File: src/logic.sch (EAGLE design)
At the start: 68 parts, among them CON1 CON-4P-TABS-JST_GH-RA, CON11 PINHEAD_1X03-2, CON12 PINHEAD_1X03-2, CON2 PINHEAD_1X04-2.54, CON3 PINHEAD_2X04-PLS-2, CON6 PINHEAD_2X02-PTH-2-MALE, CON7 PINHEAD_2X02-PTH-2-MALE, IC1 STM32F105RCT6, IC10 LM75-TSSOP8, IC11 LM75-TSSOP8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

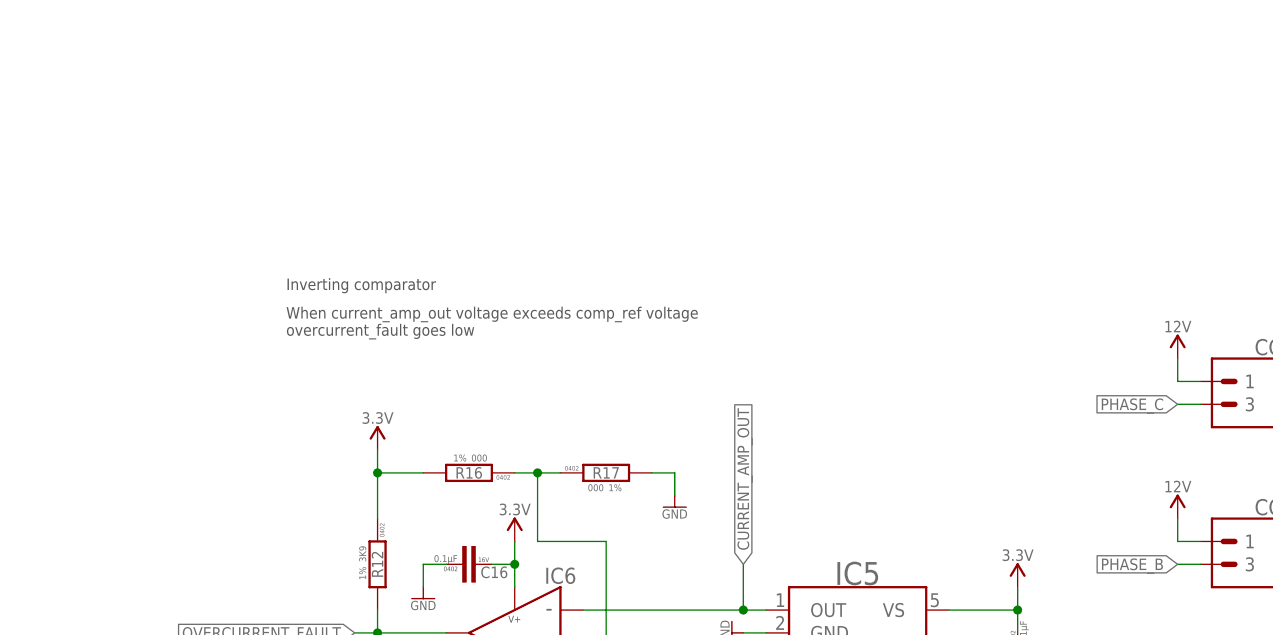
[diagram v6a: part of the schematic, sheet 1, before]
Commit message: experimental digital pot added
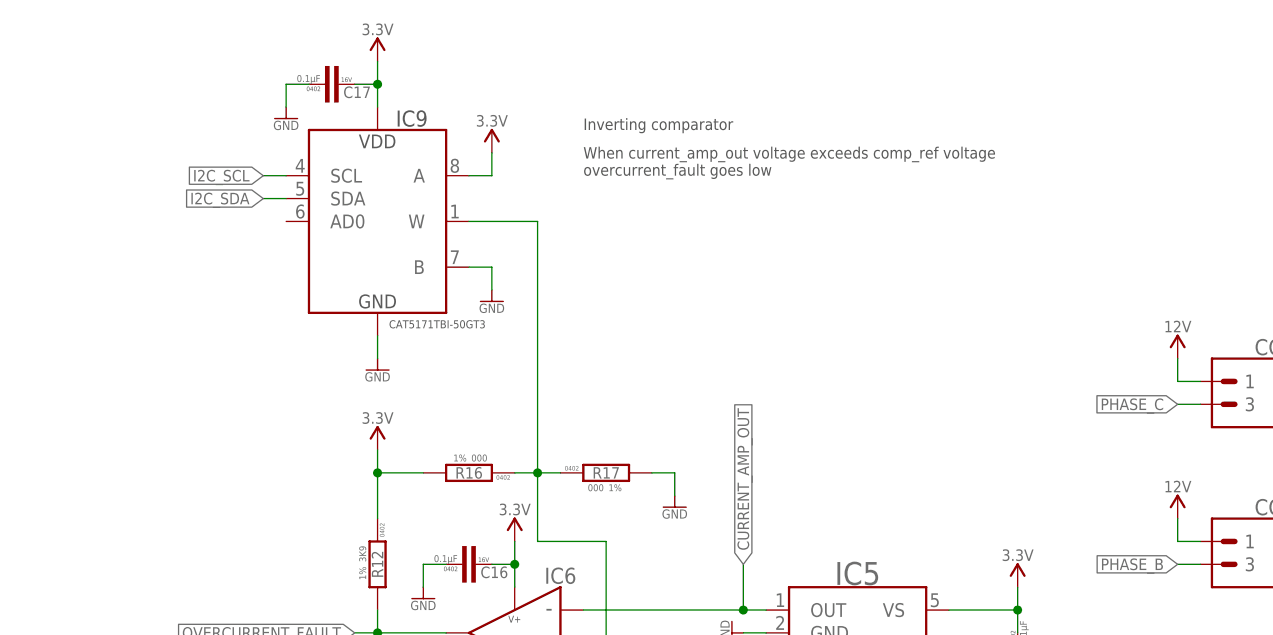
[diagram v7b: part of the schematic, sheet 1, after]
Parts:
- added C17: 0.1µF, rc:C-0402
- added IC9: CAT5171TBI-50GT3, misc:CAT5171TBI-50GT3
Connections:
- net GND: now also C17.1, IC9.B, IC9.GND
- net I2C_SCL: now also IC9.SCL
- net I2C_SDA: now also IC9.SDA
- net N$2: now also IC9.W
- net VDD_3V3: now also C17.2, IC9.A, IC9.VDD
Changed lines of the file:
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@@
 </part>
 <part name="GND44" library="supply_symbols" library_urn="urn:adsk.eagle:library:13097679" deviceset="GND" device="" value="GND"/>
+<part name="IC9" library="misc" library_urn="urn:adsk.eagle:library:5347860" deviceset="CAT5171TBI" device="" package3d_urn="urn:adsk.eagle:package:24574323/1" technology="-50GT3"/>
+<part name="C17" library="rc" library_urn="urn:adsk.eagle:library:2539423" deviceset="C" device="-0402" package3d_urn="urn:adsk.eagle:package:2539461/2" value="0.1µF">
+<attribute name="AEC-Q" value="---"/>
+<attribute name="DIGIKEY#" value="490-3261-1-ND"/>
+<attribute name="MANF" value="Murata Electronics"/>
+<attribute name="MANF#" value="GRM155R71C104KA88D"/>
+<attribute name="OPERATING_TEMP" value="-55°C ~ 125°C"/>
+<attribute name="VOLTAGE" value="16V"/>
+</part>
+<part name="P+18" library="supply_symbols" library_urn="urn:adsk.eagle:library:13097679" deviceset="3.3V" device=""/>
+<part name="GND45" library="supply_symbols" library_urn="urn:adsk.eagle:library:13097679" deviceset="GND" device="" value="GND"/>
+<part name="GND46" library="supply_symbols" library_urn="urn:adsk.eagle:library:13097679" deviceset="GND" device="" value="GND"/>
+<part name="GND47" library="supply_symbols" library_urn="urn:adsk.eagle:library:13097679" deviceset="GND" device="" value="GND"/>
+<part name="P+19" library="supply_symbols" library_urn="urn:adsk.eagle:library:13097679" deviceset="3.3V" device=""/>
 </parts>
 <sheets>
@@
 <text x="142.24" y="55.88" size="1.27" layer="97" font="vector">Place R26 TO WRITE PROTECT</text>
 <text x="142.24" y="33.02" size="1.778" layer="97">WP pin pull up is optional</text>
-<text x="96.52" y="226.06" size="1.27" layer="97" font="vector">Inverting comparator</text>
-<text x="96.52" y="220.98" size="1.27" layer="97" font="vector">When current_amp_out voltage exceeds comp_ref voltage
+<text x="129.54" y="243.84" size="1.27" layer="97" font="vector">Inverting comparator</text>
+<text x="129.54" y="238.76" size="1.27" layer="97" font="vector">When current_amp_out voltage exceeds comp_ref voltage
 overcurrent_fault goes low</text>
 </plain>
@@
 <instance part="GND44" gate="1" x="139.7" y="203.2" smashed="yes">
 <attribute name="VALUE" x="139.7" y="201.168" size="1.016" layer="96" font="vector" ratio="15" align="center"/>
+</instance>
+<instance part="IC9" gate="G$1" x="99.06" y="223.52" smashed="yes">
+<attribute name="NAME" x="110.49" y="245.11" size="1.778" layer="97" font="vector" ratio="15" align="center"/>
+<attribute name="MANF#" x="107.95" y="222.25" size="0.889" layer="97" font="vector" ratio="15" align="center-left"/>
+</instance>
+<instance part="C17" gate="G$1" x="101.6" y="248.92" smashed="yes">
+<attribute name="NAME" x="102.87" y="248.031" size="1.27" layer="95" font="vector" align="center-left"/>
+<attribute name="VALUE" x="100.33" y="249.174" size="0.762" layer="96" font="vector" align="bottom-right"/>
+<attribute name="PACKAGE" x="99.568" y="248.412" size="0.508" layer="97" font="vector" rot="R180" align="center"/>
+<attribute name="VOLTAGE" x="102.616" y="249.428" size="0.508" layer="97" font="vector" align="center-left"/>
+</instance>
+<instance part="P+18" gate="G$1" x="106.68" y="251.46" smashed="yes" rot="MR0">
+<attribute name="VALUE" x="106.68" y="255.016" size="1.27" layer="96" font="vector" ratio="15" rot="MR0" align="center"/>
+</instance>
+<instance part="GND45" gate="1" x="106.68" y="218.44" smashed="yes">
+<attribute name="VALUE" x="106.68" y="216.408" size="1.016" layer="96" font="vector" ratio="15" align="center"/>
+</instance>
+<instance part="GND46" gate="1" x="96.52" y="246.38" smashed="yes">
+<attribute name="VALUE" x="96.52" y="244.348" size="1.016" layer="96" font="vector" ratio="15" align="center"/>
+</instance>
+<instance part="GND47" gate="1" x="119.38" y="226.06" smashed="yes">
+<attribute name="VALUE" x="119.38" y="224.028" size="1.016" layer="96" font="vector" ratio="15" align="center"/>
+</instance>
+<instance part="P+19" gate="G$1" x="119.38" y="241.3" smashed="yes" rot="MR0">
+<attribute name="VALUE" x="119.38" y="244.856" size="1.27" layer="96" font="vector" ratio="15" rot="MR0" align="center"/>
 </instance>
 </instances>
@@
 <wire x1="139.7" y1="203.2" x2="139.7" y2="205.74" width="0.1524" layer="91"/>
 <wire x1="139.7" y1="205.74" x2="137.16" y2="205.74" width="0.1524" layer="91"/>
+</segment>
+<segment>
+<pinref part="GND45" gate="1" pin="GND"/>
+<pinref part="IC9" gate="G$1" pin="GND"/>
+<wire x1="106.68" y1="218.44" x2="106.68" y2="220.98" width="0.1524" layer="91"/>
+</segment>
+<segment>
+<pinref part="GND46" gate="1" pin="GND"/>
+<wire x1="96.52" y1="246.38" x2="96.52" y2="248.92" width="0.1524" layer="91"/>
+<pinref part="C17" gate="G$1" pin="1"/>
+<wire x1="96.52" y1="248.92" x2="99.06" y2="248.92" width="0.1524" layer="91"/>
+</segment>
+<segment>
+<pinref part="GND47" gate="1" pin="GND"/>
+<wire x1="119.38" y1="226.06" x2="119.38" y2="228.6" width="0.1524" layer="91"/>
+<pinref part="IC9" gate="G$1" pin="B"/>
+<wire x1="119.38" y1="228.6" x2="116.84" y2="228.6" width="0.1524" layer="91"/>
 </segment>
 </net>
@@
 <label x="149.86" y="50.8" size="1.27" layer="95" rot="R180" xref="yes"/>
 </segment>
+<segment>
+<pinref part="IC9" gate="G$1" pin="SCL"/>
+<wire x1="96.52" y1="238.76" x2="93.98" y2="238.76" width="0.1524" layer="91"/>
+<label x="93.98" y="238.76" size="1.27" layer="95" rot="R180" xref="yes"/>
+</segment>
 </net>
 <net name="I2C_SDA" class="0">
@@
 <wire x1="152.4" y1="40.64" x2="149.86" y2="40.64" width="0.1524" layer="91"/>
 <label x="149.86" y="40.64" size="1.27" layer="95" rot="R180" xref="yes"/>
+</segment>
+<segment>
+<pinref part="IC9" gate="G$1" pin="SDA"/>
+<wire x1="96.52" y1="236.22" x2="93.98" y2="236.22" width="0.1524" layer="91"/>
+<label x="93.98" y="236.22" size="1.27" layer="95" rot="R180" xref="yes"/>
 </segment>
 </net>
@@
 <junction x="106.68" y="205.74"/>
 </segment>
+<segment>
+<pinref part="IC9" gate="G$1" pin="VDD"/>
+<wire x1="106.68" y1="246.38" x2="106.68" y2="248.92" width="0.1524" layer="91"/>
+<pinref part="C17" gate="G$1" pin="2"/>
+<wire x1="106.68" y1="248.92" x2="104.14" y2="248.92" width="0.1524" layer="91"/>
+<wire x1="106.68" y1="248.92" x2="106.68" y2="251.46" width="0.1524" layer="91"/>
+<junction x="106.68" y="248.92"/>
+<pinref part="P+18" gate="G$1" pin="VDD_3V3"/>
+</segment>
+<segment>
+<pinref part="P+19" gate="G$1" pin="VDD_3V3"/>
+<wire x1="119.38" y1="241.3" x2="119.38" y2="238.76" width="0.1524" layer="91"/>
+<pinref part="IC9" gate="G$1" pin="A"/>
+<wire x1="119.38" y1="238.76" x2="116.84" y2="238.76" width="0.1524" layer="91"/>
+</segment>
 </net>
 <net name="BOOT0" class="0">
@@
 <wire x1="132.08" y1="198.12" x2="132.08" y2="185.42" width="0.1524" layer="91"/>
 <junction x="132.08" y="185.42"/>
-</segment>
-</net>
+<pinref part="IC9" gate="G$1" pin="W"/>
+<wire x1="116.84" y1="233.68" x2="124.46" y2="233.68" width="0.1524" layer="91"/>
+<wire x1="124.46" y1="233.68" x2="124.46" y2="205.74" width="0.1524" layer="91"/>
+</segment>
+</net>

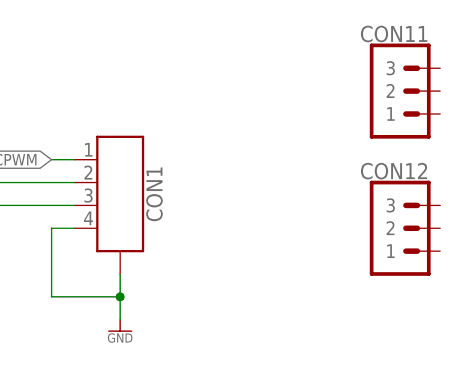
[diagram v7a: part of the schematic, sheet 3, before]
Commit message: bigger connector PCB connectors
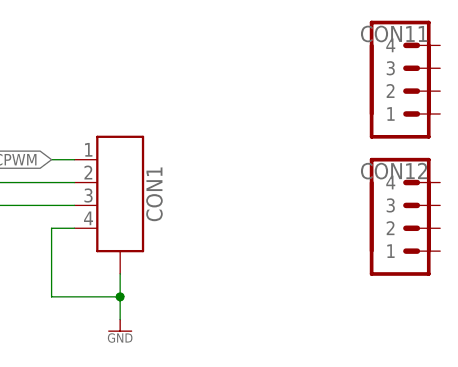
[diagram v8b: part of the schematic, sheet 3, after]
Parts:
- CON11, CON12: value PINHEAD_1X03-2 -> PINHEAD_1X04-2; device pinhead:PINHEAD_1X03-2 -> pinhead:PINHEAD_1X04-2
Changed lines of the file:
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@@
 <part name="+P12" library="supply_symbols" library_urn="urn:adsk.eagle:library:13097679" deviceset="3.3V" device=""/>
 <part name="GND41" library="supply_symbols" library_urn="urn:adsk.eagle:library:13097679" deviceset="GND" device="" value="GND"/>
-<part name="CON11" library="pinhead" library_urn="urn:adsk.eagle:library:2540341" deviceset="PINHEAD_1X03" device="-2" package3d_urn="urn:adsk.eagle:package:4854341/3"/>
-<part name="CON12" library="pinhead" library_urn="urn:adsk.eagle:library:2540341" deviceset="PINHEAD_1X03" device="-2" package3d_urn="urn:adsk.eagle:package:4854341/3"/>
+<part name="CON11" library="pinhead" library_urn="urn:adsk.eagle:library:2540341" deviceset="PINHEAD_1X04" device="-2" package3d_urn="urn:adsk.eagle:package:4854340/4"/>
+<part name="CON12" library="pinhead" library_urn="urn:adsk.eagle:library:2540341" deviceset="PINHEAD_1X04" device="-2" package3d_urn="urn:adsk.eagle:package:4854340/4"/>
 <part name="CON3" library="pinhead" library_urn="urn:adsk.eagle:library:2540341" deviceset="PINHEAD_2X04" device="-PLS-2" package3d_urn="urn:adsk.eagle:package:23823581/1"/>
 <part name="IC8" library="misc" library_urn="urn:adsk.eagle:library:5347860" deviceset="LM75" device="-TSSOP8" package3d_urn="urn:adsk.eagle:package:7691413/6">
